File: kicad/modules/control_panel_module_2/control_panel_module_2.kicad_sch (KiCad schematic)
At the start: 2 parts, among them J1 Screw_Terminal_01x06, J2 Screw_Terminal_01x06

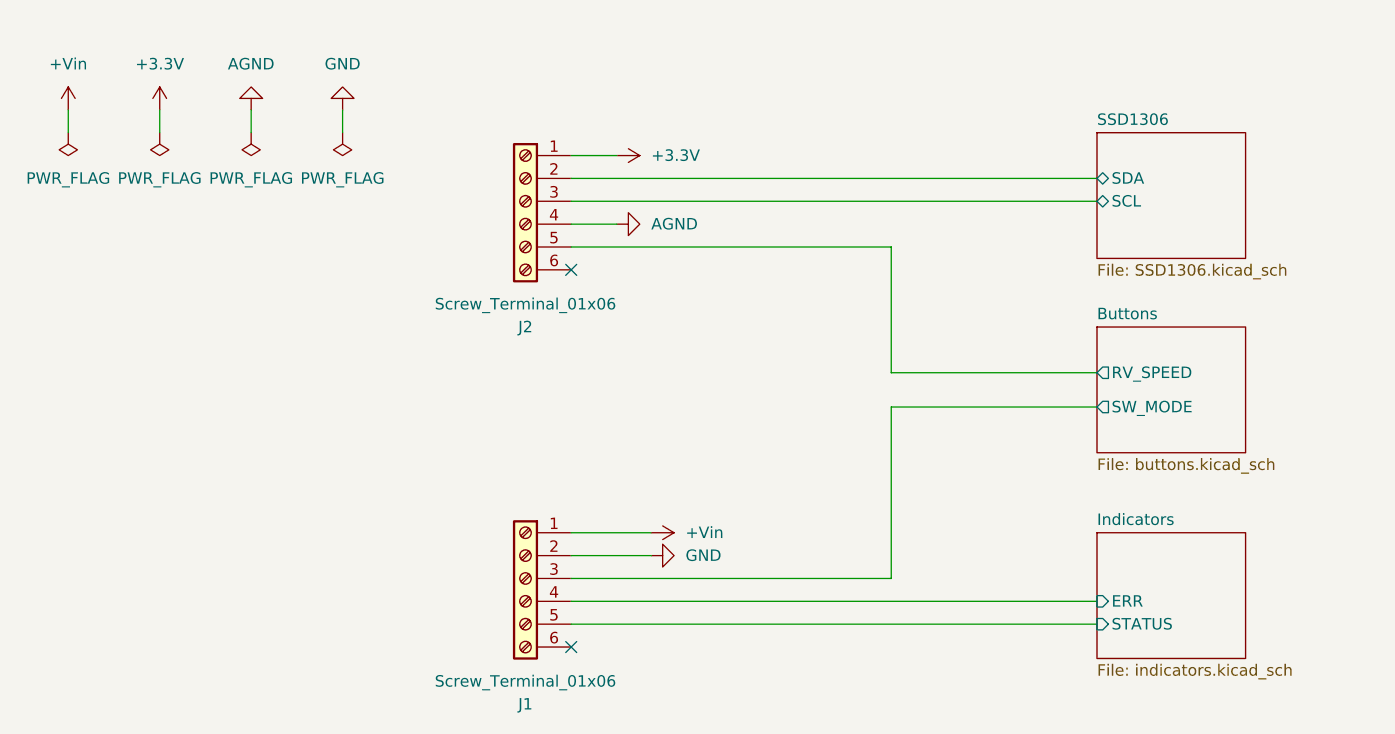
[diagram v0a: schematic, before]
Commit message: Connector for bigger current, control module 2
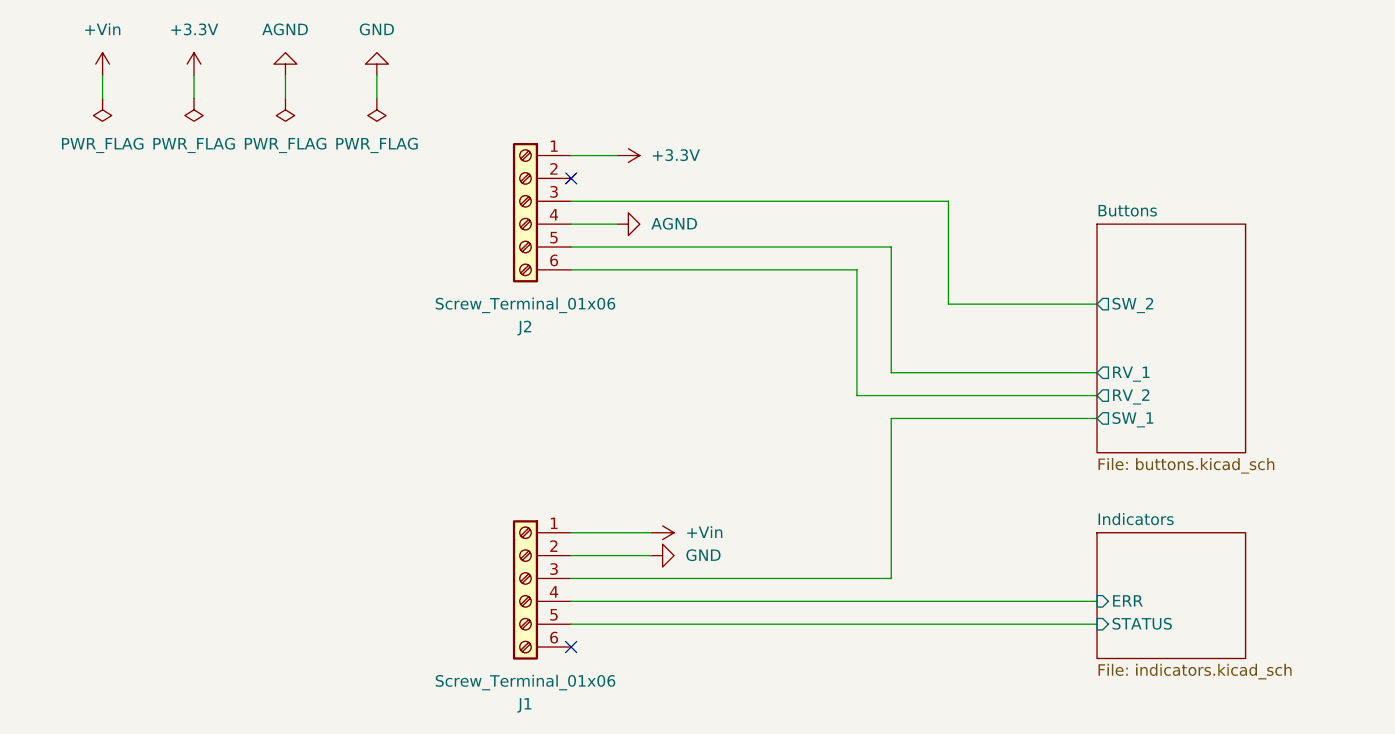
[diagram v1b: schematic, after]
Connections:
- net Buttons/RV_2: now reaches J2.6 (Pin_6)
- net Buttons/RV_SPEED renamed Buttons/RV_1
- net Buttons/SW_MODE renamed Buttons/SW_1
- net SSD1306/SCL renamed Buttons/SW_2
- net SSD1306/SDA: no longer names the net of J2.2 (Pin_2)
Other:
- removed sheet SSD1306
- sheet Buttons ports: added RV_1, RV_2, SW_1, SW_2; removed RV_SPEED, SW_MODE

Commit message: Add part numbers
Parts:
- J1, J2: value Screw_Terminal_01x06 -> 1x6 2.54; Manufacturer Part Number (none) -> 68000-420HLF; Mouser number (none) -> 649-68000-420HLF
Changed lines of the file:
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@@
 			)
 		)
-		(property "Value" "Screw_Terminal_01x06"
+		(property "Value" "1x6 2.54"
 			(at 68.58 91.44 0)
 			(effects
@@
 			)
 		)
-		(property "Description" "Generic screw terminal, single row, 01x06, script generated (kicad-library-utils/schlib/autogen/connector/)"
-			(at 68.58 80.01 0)
-			(effects
-				(font
-					(size 1.27 1.27)
-				)
-				(hide yes)
-			)
-		)
-		(property "Manufacturer Part Number" ""
-			(at 68.58 80.01 0)
-			(effects
-				(font
-					(size 1.27 1.27)
-				)
-				(hide yes)
-			)
-		)
-		(property "Mouser number" ""
+		(property "Description" "CUSTOM"
+			(at 68.58 80.01 0)
+			(effects
+				(font
+					(size 1.27 1.27)
+				)
+				(hide yes)
+			)
+		)
+		(property "Manufacturer Part Number" "68000-420HLF"
+			(at 68.58 80.01 0)
+			(effects
+				(font
+					(size 1.27 1.27)
+				)
+				(hide yes)
+			)
+		)
+		(property "Mouser number" "649-68000-420HLF"
 			(at 68.58 80.01 0)
 			(effects
@@
 			)
 		)
-		(property "Value" "Screw_Terminal_01x06"
+		(property "Value" "1x6 2.54"
 			(at 68.58 49.53 0)
 			(effects
@@
 			)
 		)
-		(property "Description" "Generic screw terminal, single row, 01x06, script generated (kicad-library-utils/schlib/autogen/connector/)"
-			(at 68.58 38.1 0)
-			(effects
-				(font
-					(size 1.27 1.27)
-				)
-				(hide yes)
-			)
-		)
-		(property "Manufacturer Part Number" ""
-			(at 68.58 38.1 0)
-			(effects
-				(font
-					(size 1.27 1.27)
-				)
-				(hide yes)
-			)
-		)
-		(property "Mouser number" ""
-			(at 68.58 38.1 0)
-			(effects
+		(property "Description" "CUSTOM"
+			(at 68.58 38.1 0)
+			(effects
+				(font
+					(size 1.27 1.27)
+				)
+				(hide yes)
+			)
+		)
+		(property "Manufacturer Part Number" "68000-420HLF"
+			(at 68.58 38.1 0)
+			(effects
+				(font
+					(size 1.27 1.27)
+				)
+				(hide yes)
+			)
+		)
+		(property "Mouser number" "649-68000-420HLF"
+			(at 68.58 38.1 0)
+			(effects
